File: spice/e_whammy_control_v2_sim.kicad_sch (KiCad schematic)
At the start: 31 parts, among them U1 ${SIM.PARAMS}, U2 ${SIM.PARAMS}, U3 ADG779, U4 OPEN_COLLECTOR_COMPARATOR, U5 OPEN_COLLECTOR_COMPARATOR, U6 SCHMITT_MUX

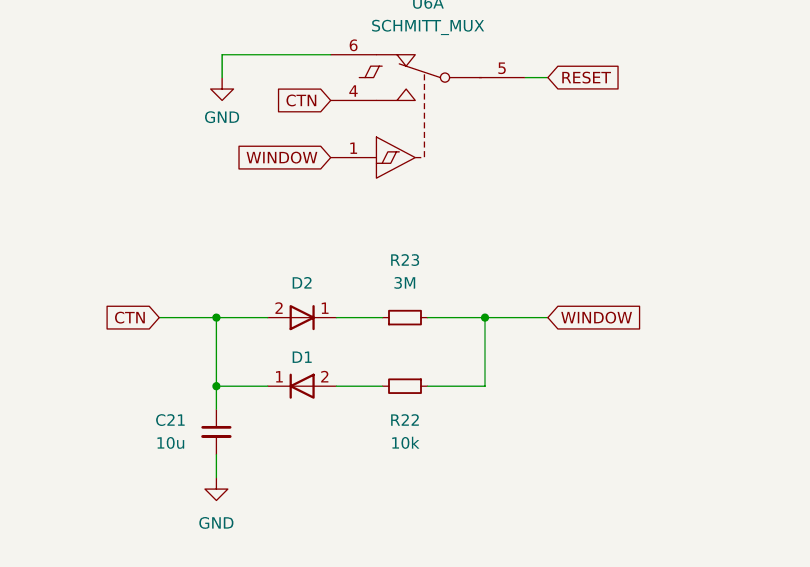
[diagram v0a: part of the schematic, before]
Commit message: e-Whammy: retune latch-up timeout 20s->16s (R23 3M->2.4M)
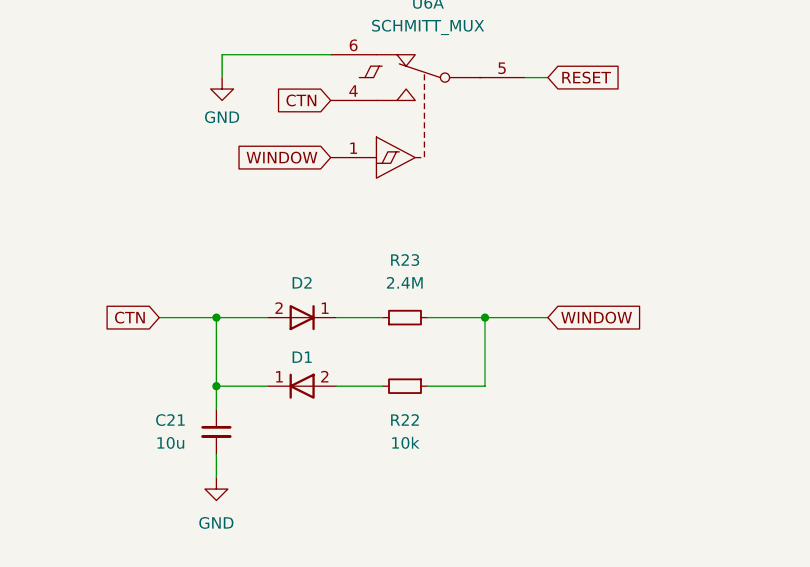
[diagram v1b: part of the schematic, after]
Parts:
- R23: value 3M -> 2.4M
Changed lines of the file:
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@@
 			)
 		)
-		(property "Value" "3M"
+		(property "Value" "2.4M"
 			(at 191.135 127 90)
 			(effects
